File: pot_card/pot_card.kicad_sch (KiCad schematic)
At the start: 27 parts, among them U1 LM317EMPX/NOPB, U2 LM321

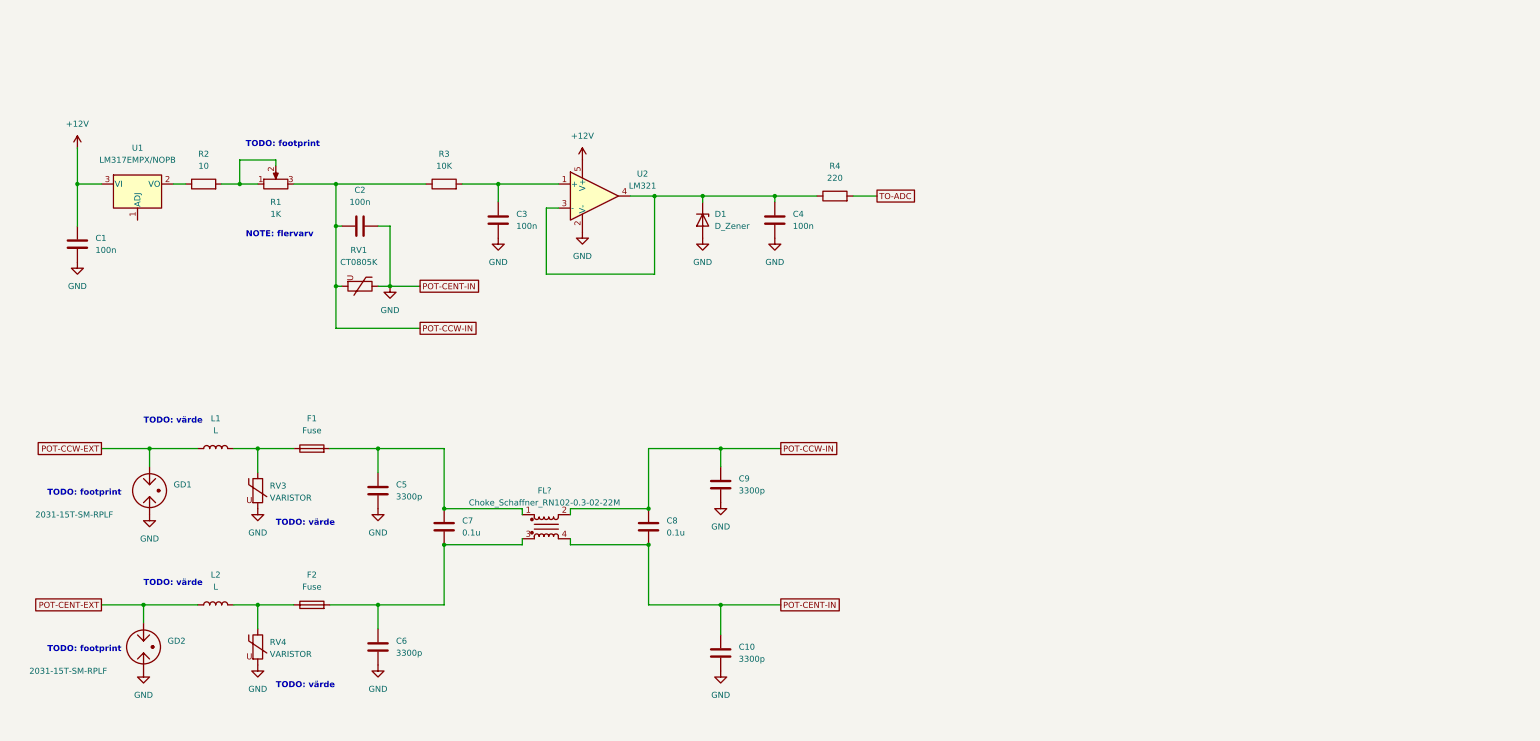
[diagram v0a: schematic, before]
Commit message: Remove ERC Errors/Warnings, Misc changes
Add connectors for signals
Add power flag to power nets
Add resistor to vreg input of regulator
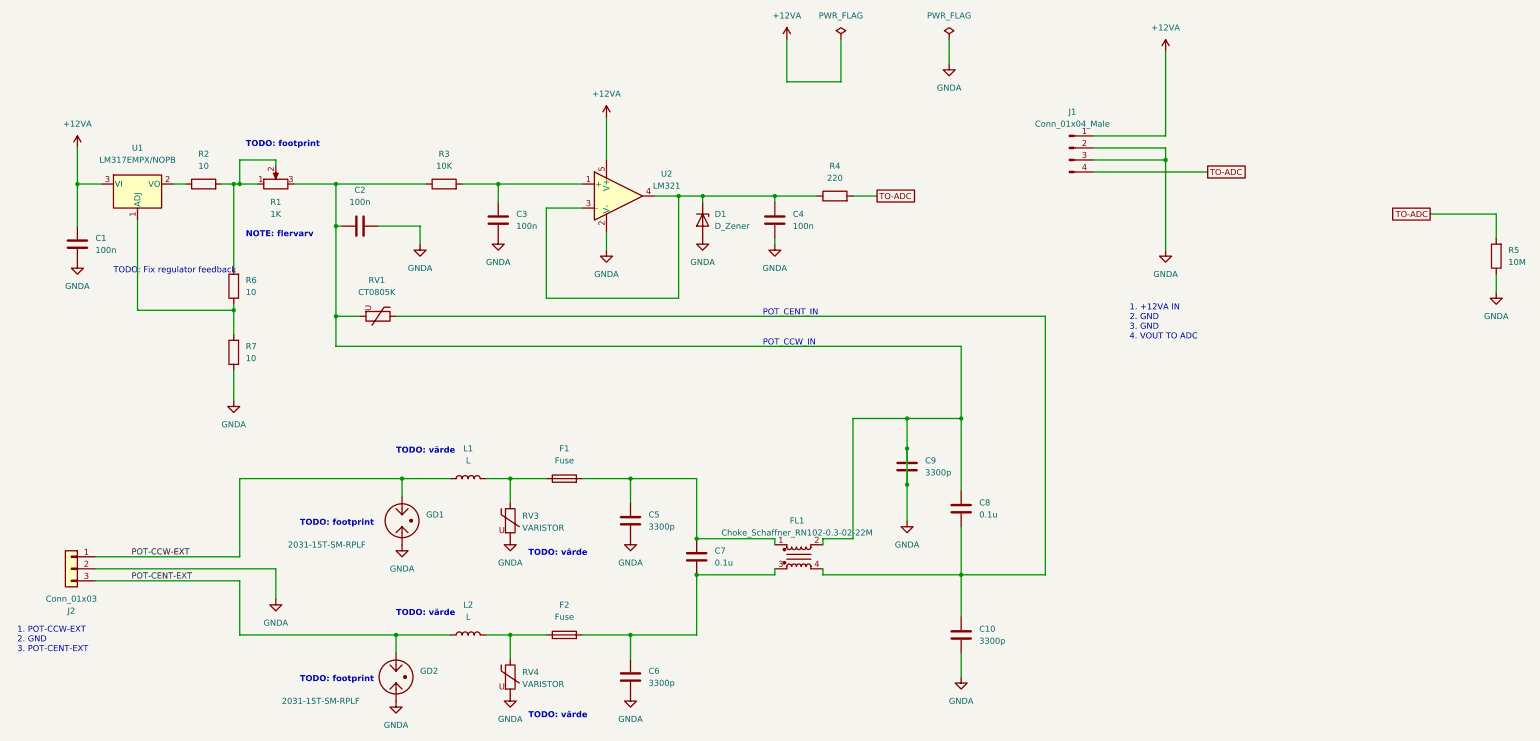
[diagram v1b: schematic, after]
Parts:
- added J1: Conn_01x04_Male, Connector_JST:JST_XH_B4B-XH-AM_1x04_P2.50mm_Vertical, symbol Connector:Conn_01x04_Male
- added J2: Conn_01x03, Connector_JST:JST_XH_B3B-XH-AM_1x03_P2.50mm_Vertical, symbol Connector_Generic:Conn_01x03
- added R5: 10M, Resistor_SMD:R_0805_2012Metric, symbol Device:R
- added R6, R7: 10, Resistor_SMD:R_0805_2012Metric, symbol Device:R
- gave numbers to parts that had none: 1
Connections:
- net POT-CCW-IN is gone; now on net GNDA: C2.1, C8.1, C9.1, FL1.2, R1.3, R3.1, RV1.2
- net POT-CCW-EXT: now also J2.1 (Pin_1)
- net POT-CENT-EXT: now also J2.3 (Pin_3)
- net TO-ADC: now also J1.4 (Pin_4), R5.2
- net at R1.1, R1.2, R2.2: now also R6.2
- net at U1.1 (ADJ): now also R6.1, R7.2
- net +12V renamed +12VA
- net +12VA: now also J1.1 (Pin_1)
- net GND renamed GNDA
- net GNDA: now also J1.2 (Pin_2), J1.3 (Pin_3), J2.2 (Pin_2), R5.1, R7.1; no longer C10.1, C8.2, FL1.4, RV1.1
- new net: C10.1, C8.2, FL1.4, RV1.1
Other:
- note added: "1. +12VA IN 2. GND 3. GND 4. VOUT TO ADC"
- note added: "1. POT-CCW-EXT 2. GND 3. POT-CENT-EXT"
- note added: "POT_CCW_IN"
- note added: "POT_CENT_IN"
- note added: "TODO: Fix regulator feedback"
- moved on the sheet: C5, C6, C7, C8, F1, F2, FL1, GD1, GD2, L1, L2, RV1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
